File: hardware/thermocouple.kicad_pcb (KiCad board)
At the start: 2 copper layers, 32.5 x 25 mm, 23 parts, among them J101 AKL_5_2, P101 CON-SENSOR, U101 M24C64, U102 MAX31856, U103 DRILL, U104 DRILL, U105 DRILL, U106 DRILL

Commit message: add fiducials to pcb
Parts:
- added Fiducial_Mark: VAL**, kicad-libraries:Fiducial_Mark, F.Cu at (161.6, 149.4)
- added Fiducial_Mark: VAL**, kicad-libraries:Fiducial_Mark, F.Cu at (175.1, 130.4)
- added Fiducial_Mark: VAL**, kicad-libraries:Fiducial_Mark, F.Cu at (180.6, 149.4)
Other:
- board text added: "Thermocouple 1.0"
- board text removed: "Thermocouple"

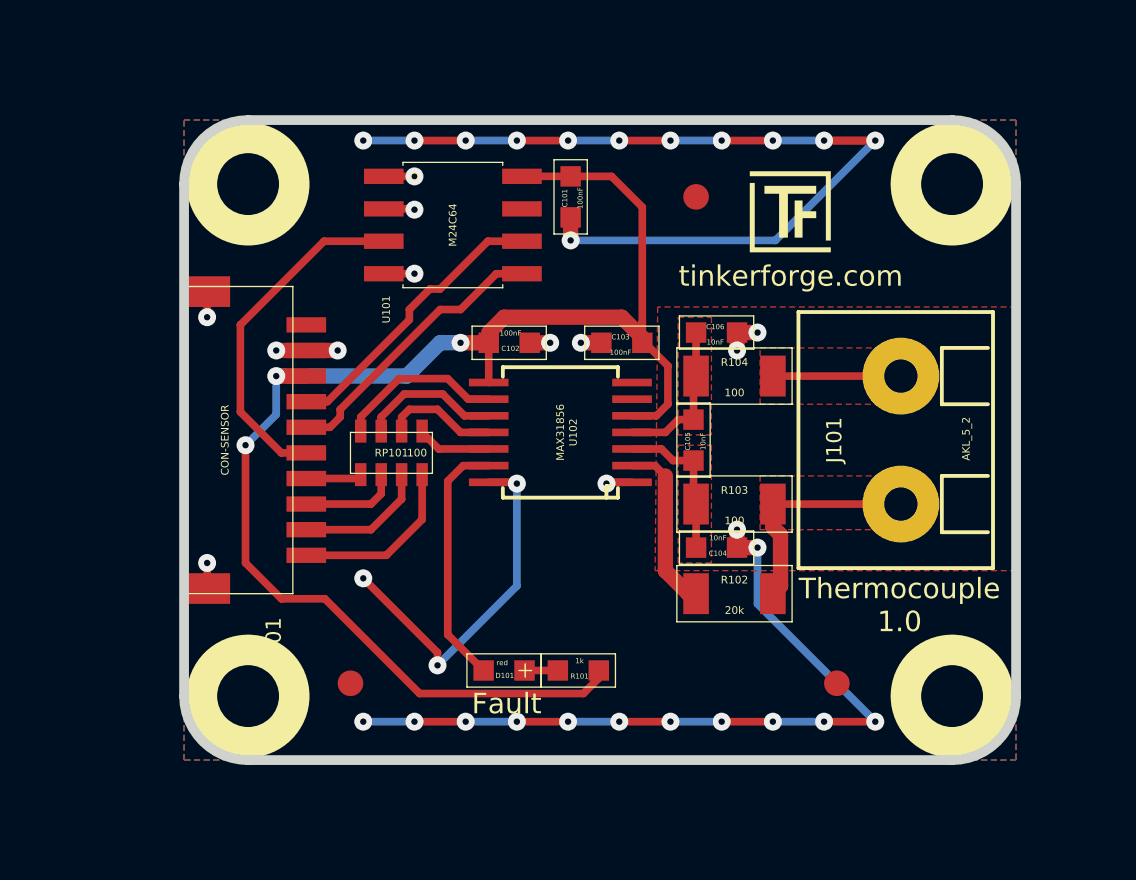
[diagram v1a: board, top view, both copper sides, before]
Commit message: fit size to 5mm grid
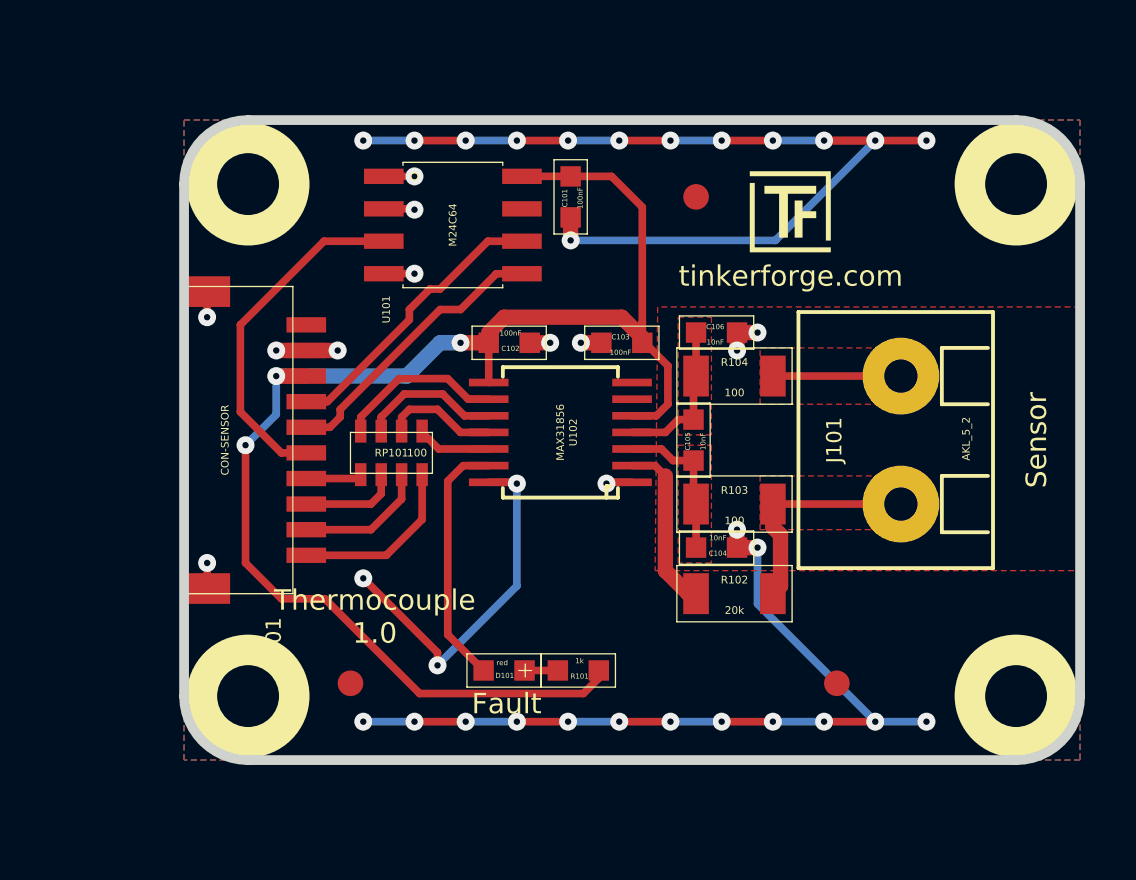
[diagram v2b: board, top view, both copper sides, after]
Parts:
- moved U105 2.50 mm to (187.6, 149.9)
- moved U106 2.50 mm to (187.6, 129.9)
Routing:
- net GND: track 92.9 -> 96.9 mm, vias 40 -> 42
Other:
- board size 32.5 x 25 mm -> 35 x 25 mm
- board text added: "Sensor"

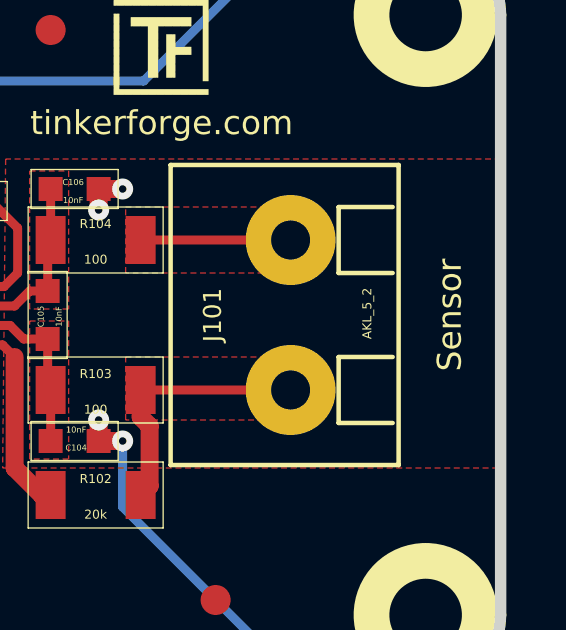
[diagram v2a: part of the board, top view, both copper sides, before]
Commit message: add polarity description
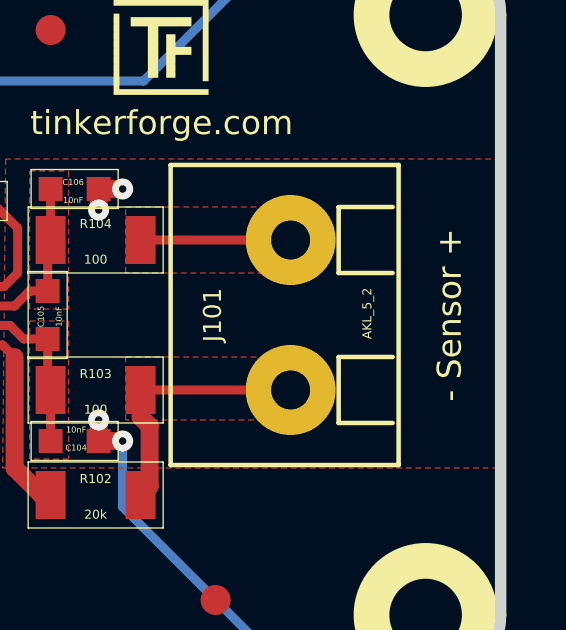
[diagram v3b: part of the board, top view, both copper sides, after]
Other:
- board text added: "- Sensor +"
- board text removed: "Sensor"

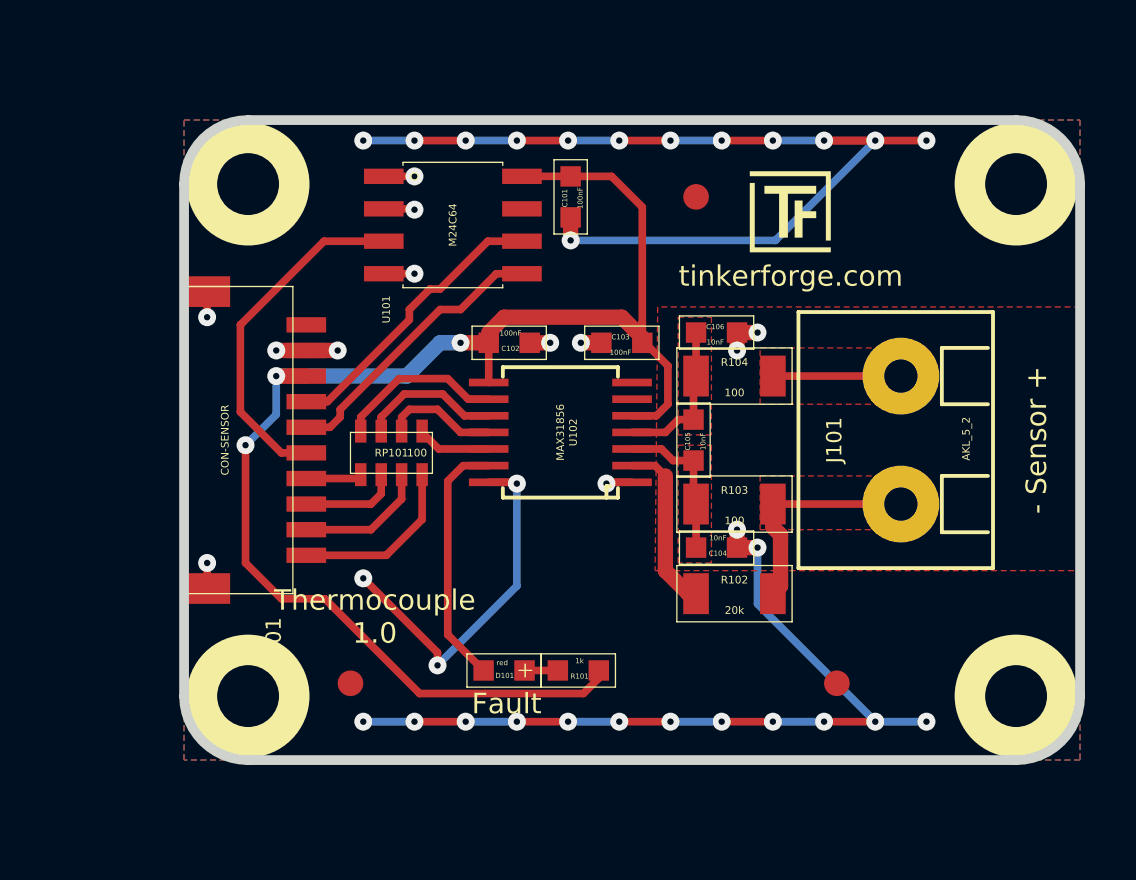
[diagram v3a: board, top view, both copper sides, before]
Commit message: change terminal block to thermocouple connector
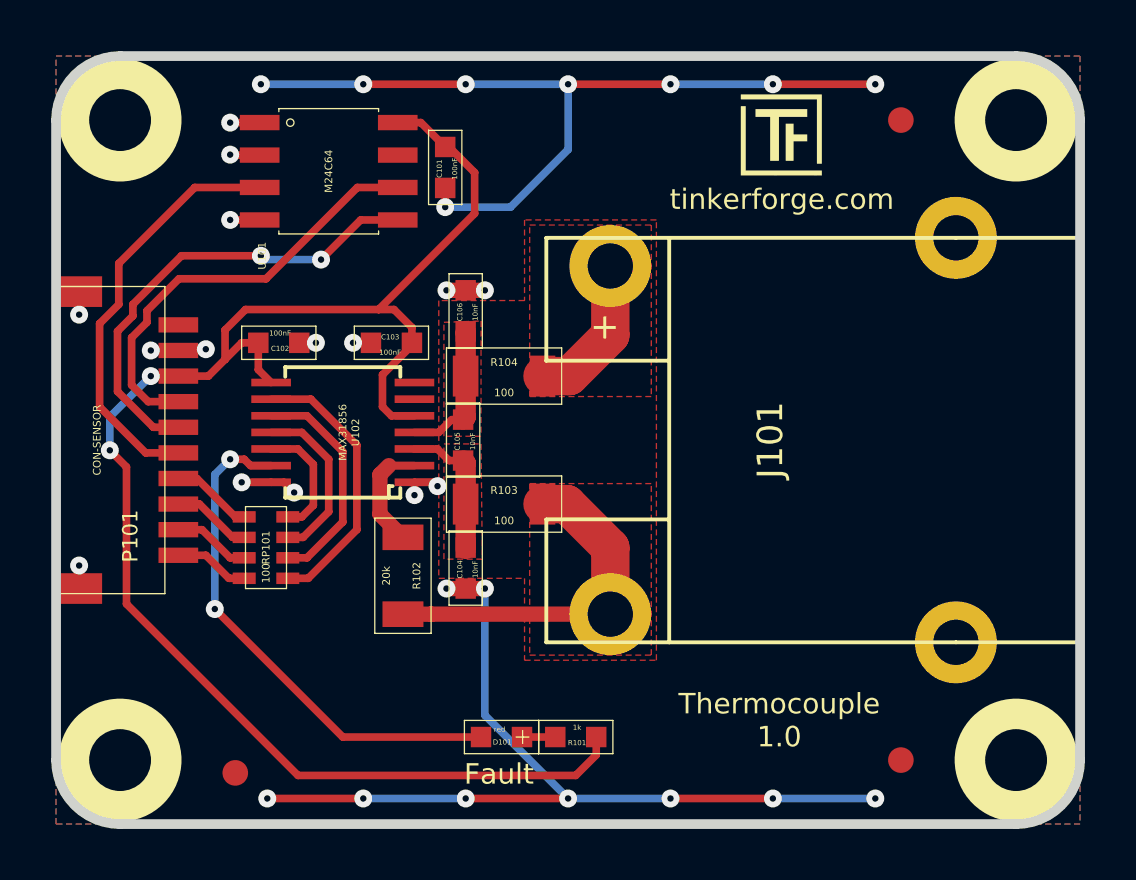
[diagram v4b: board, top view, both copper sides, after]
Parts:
- J101: footprint kicad-libraries:AKL_5_2 -> kicad-libraries:PCC_SMP
- moved R102 13.0 mm to (163.7, 145.2), turned to 90 degrees
- moved C106 9.84 mm to (166.1, 134.9), turned to 270 degrees
- moved C104 9.83 mm to (166.1, 144.9), turned to 270 degrees
- moved C102 9.00 mm to (158.8, 136.1)
- moved C103 9.00 mm to (163.2, 136.1)
- moved C105 9.00 mm to (166.0, 139.9)
- moved R103 9.00 mm to (167.6, 142.4)
- moved R104 9.00 mm to (167.6, 137.4)
- moved Fiducial_Mark 8.54 mm to (183.1, 127.4)
- moved U102 8.50 mm to (161.3, 139.6)
- moved RP101 6.14 mm to (158.3, 144.1), turned to 270 degrees
- moved Fiducial_Mark 5.70 mm to (157.1, 152.9)
- moved U103 5.59 mm to (152.6, 127.4)
- moved U104 5.59 mm to (152.6, 152.4)
- moved U101 5.29 mm to (160.8, 129.4)
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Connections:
- U102 pad 10: Net-(RP101-Pad3) -> Net-(RP101-Pad2)
- U102 pad 11: Net-(RP101-Pad2) -> Net-(RP101-Pad3)
- U102 pad 12: Net-(RP101-Pad1) -> Net-(RP101-Pad4)
- U102 pad 9: Net-(RP101-Pad4) -> Net-(RP101-Pad1)
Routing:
- net GND: track 96.9 -> 81.8 mm, vias 42 -> 32
- net Net-(D101-Pad2): track 9.83 -> 20.3 mm, vias 0 -> 2
- net Net-(RP101-Pad1): track 2.92 -> 10.9 mm
- net Net-(P101-Pad5): track 11.1 -> 18.4 mm, vias 0 -> 2
- net VCC: track 58.0 -> 63.9 mm, vias 3 -> 2
- net Net-(P101-Pad4): track 11.3 -> 17.0 mm
- net Net-(J101-Pad2): track 8.75 -> 14.3 mm
- net Net-(RP101-Pad2): track 4.45 -> 8.86 mm
- net Net-(P101-Pad10): track 6.85 -> 2.95 mm
- net Net-(P101-Pad6): track 13.6 -> 16.5 mm
- net Net-(R102-Pad2): track 6.74 -> 4.32 mm
- net Net-(P101-Pad9): track 5.17 -> 3.03 mm
- net Net-(RP101-Pad4): track 6.50 -> 4.68 mm
- net Net-(RP101-Pad3): track 5.48 -> 6.75 mm
- net Net-(J101-Pad1): track 5.00 -> 6.01 mm
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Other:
- board size 35 x 25 mm -> 40 x 30 mm
- board text removed: "- Sensor +"
